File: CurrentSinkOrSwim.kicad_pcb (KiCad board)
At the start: 2 copper layers, 23 parts, among them P101 CONN_01X02, P102 CONN_01X03, P103 CONN_01X02, Q201 BUK9575, U201 LMV358IDT, U301 LMV358, U401 LM2931D-R

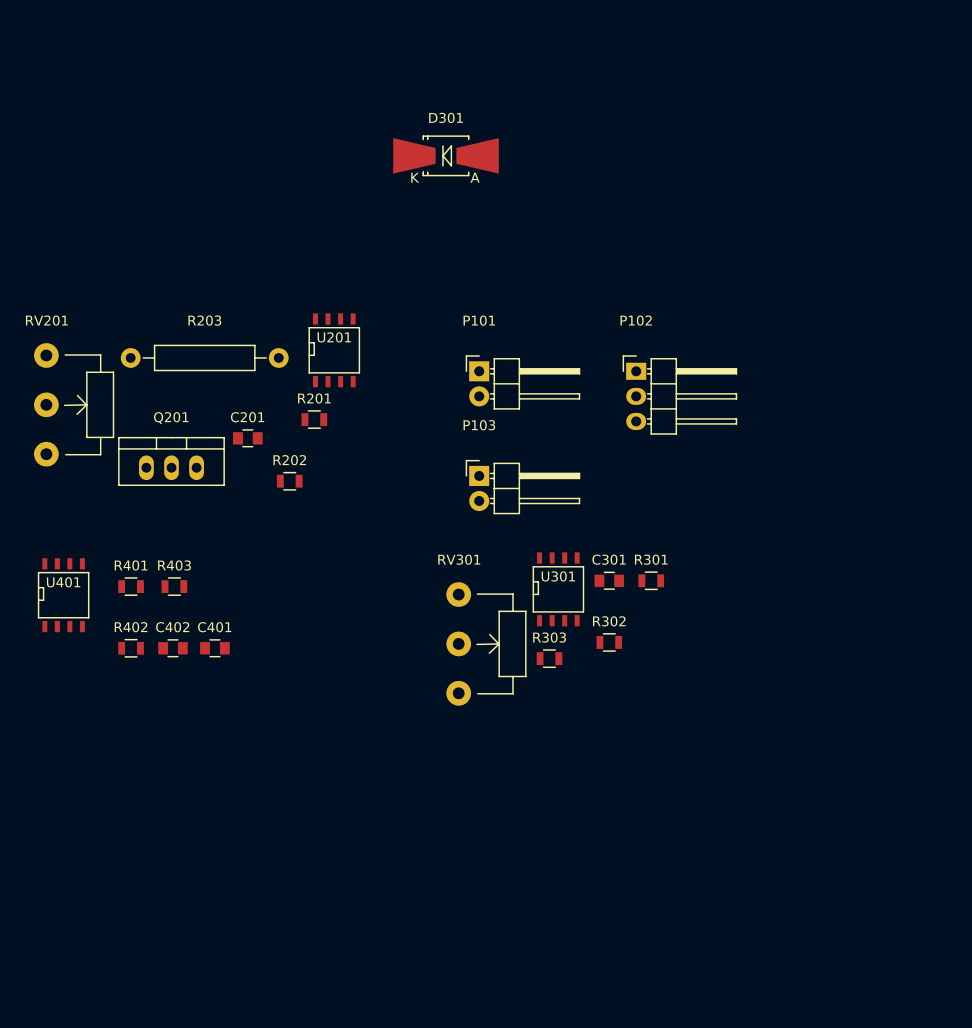
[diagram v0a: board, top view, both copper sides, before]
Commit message: Add heat sink footprint
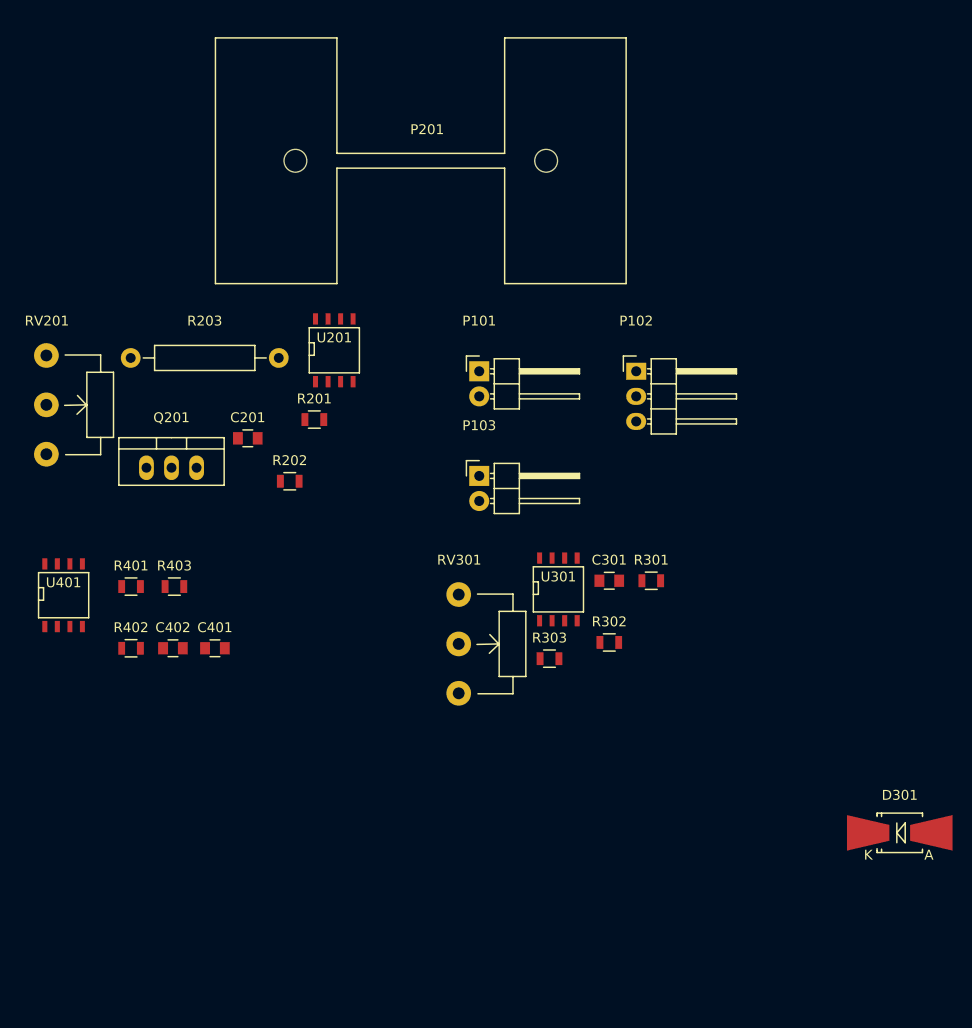
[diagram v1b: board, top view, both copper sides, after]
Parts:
- added P201: CONN_01X01, current:FA-T220-38E-ND, F.Cu at (125.5, 60.7)
- moved D301 82.6 mm to (174.0, 128.8)
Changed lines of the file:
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@@
     (tracks 0)
     (zones 0)
-    (modules 23)
+    (modules 24)
     (nets 20)
   )
@@
   )
   (module Diodes_SMD:SMB-SMC_Universal_Handsoldering (layer F.Cu)
-    (at 128.016 60.198)
+    (at 173.99 128.778)
     (descr "Diode, Universal, SMB, SMC, Handsoldering,")
     (tags "Diode Universal SMB SMC Handsoldering ")
@@
     )
   )
+  (module current:FA-T220-38E-ND (layer F.Cu)
+    (at 125.476 60.706)
+    (fp_text reference P201 (at 0.635 -3.175) (layer F.SilkS)
+      (effects (font (size 1 1) (thickness 0.15)))
+    )
+    (fp_text value CONN_01X01 (at 0 -5.715) (layer F.Fab)
+      (effects (font (size 1 1) (thickness 0.15)))
+    )
+    (fp_line (start -20.8153 12.4333) (end -8.509 12.4333) (layer F.SilkS) (width 0.15))
+    (fp_line (start 8.4836 12.4333) (end 20.7899 12.4333) (layer F.SilkS) (width 0.15))
+    (fp_line (start 8.4836 -12.4587) (end 20.7899 -12.4587) (layer F.SilkS) (width 0.15))
+    (fp_line (start -20.8153 -12.4587) (end -8.509 -12.4587) (layer F.SilkS) (width 0.15))
+    (fp_line (start 8.4836 12.4333) (end 8.4836 0.7366) (layer F.SilkS) (width 0.15))
+    (fp_line (start -8.509 12.4333) (end -8.509 0.7366) (layer F.SilkS) (width 0.15))
+    (fp_line (start -8.509 -0.762) (end -8.509 -12.4587) (layer F.SilkS) (width 0.15))
+    (fp_line (start 8.4836 -0.762) (end 8.4836 -12.4587) (layer F.SilkS) (width 0.15))
+    (fp_line (start -8.509 0.7366) (end 8.4836 0.7366) (layer F.SilkS) (width 0.15))
+    (fp_line (start -8.509 -0.762) (end 8.4836 -0.762) (layer F.SilkS) (width 0.15))
+    (fp_line (start -20.8153 -12.4587) (end -20.8153 12.4333) (layer F.SilkS) (width 0.15))
+    (fp_line (start 20.7899 12.4333) (end 20.7899 -12.4587) (layer F.SilkS) (width 0.15))
+    (pad "" np_thru_hole circle (at -12.7127 -0.0127) (size 2.3114 2.3114) (drill 2.3114) (layers *.Cu *.Mask))
+    (pad "" np_thru_hole circle (at 12.6873 -0.0127) (size 2.3114 2.3114) (drill 2.3114) (layers *.Cu *.Mask))
+  )
 )

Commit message: Remove extra erroneus LMV358
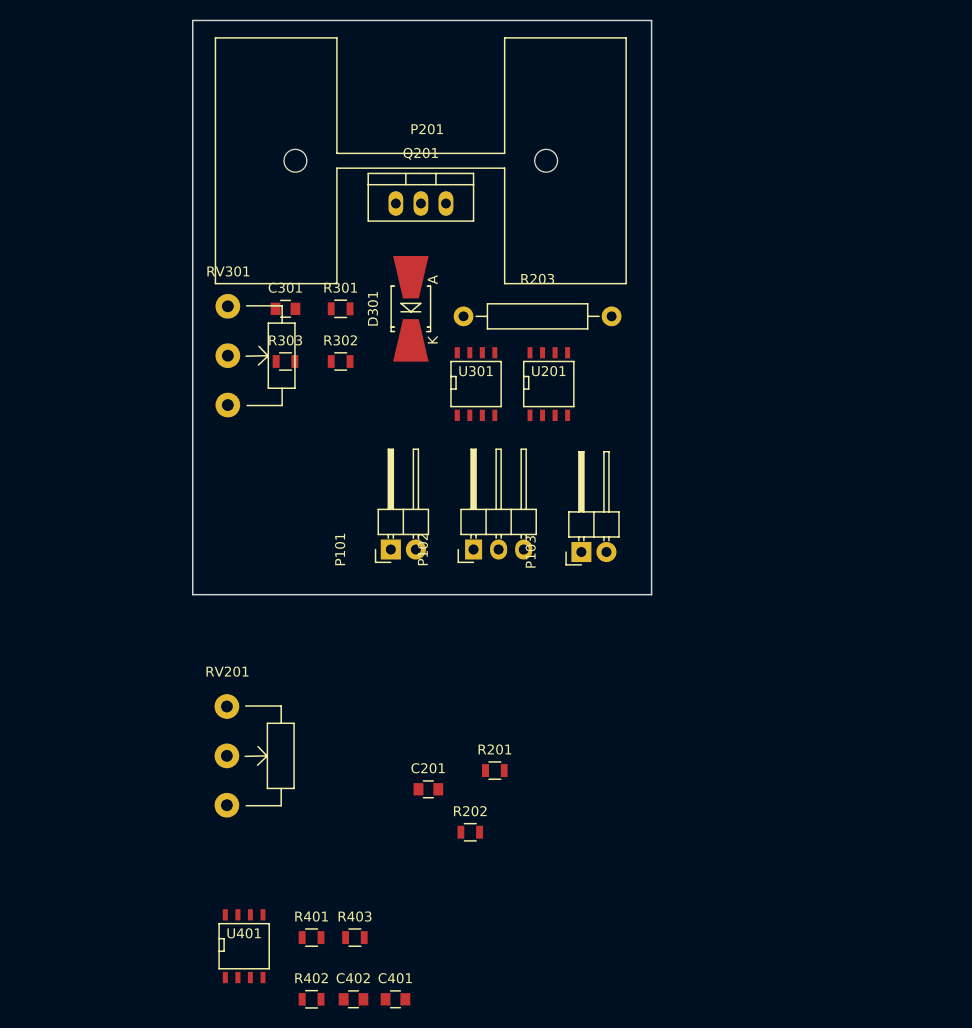
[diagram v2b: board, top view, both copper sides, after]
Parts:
- U201: value LMV358IDT -> LMV358
- moved D301 72.6 mm to (124.5, 75.7), turned to 90 degrees
- moved C301 42.8 mm to (111.8, 75.7)
- moved R301 41.8 mm to (117.3, 75.7)
- moved R303 40.3 mm to (111.8, 81.0)
- moved R201 40.0 mm to (133.0, 122.5)
- moved C401 40.0 mm to (122.9, 145.6)
- moved C402 40.0 mm to (118.6, 145.6)
- moved R202 40.0 mm to (130.5, 128.7)
- moved R401 40.0 mm to (114.4, 139.4)
- moved R402 40.0 mm to (114.4, 145.6)
- moved RV201 40.0 mm to (105.8, 116.0)
- moved C201 40.0 mm to (126.2, 124.4)
- moved R403 40.0 mm to (118.8, 139.4)
- moved U401 40.0 mm to (107.6, 140.3)
- moved R302 39.4 mm to (117.3, 81.0)
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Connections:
- U201 pad 5: (no net) -> Net-(R301-Pad1)
- U201 pad 6: (no net) -> Net-(R302-Pad2)
- U201 pad 7: (no net) -> Net-(D301-Pad1)
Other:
- board outline added: 46.5 x 58.2 mm

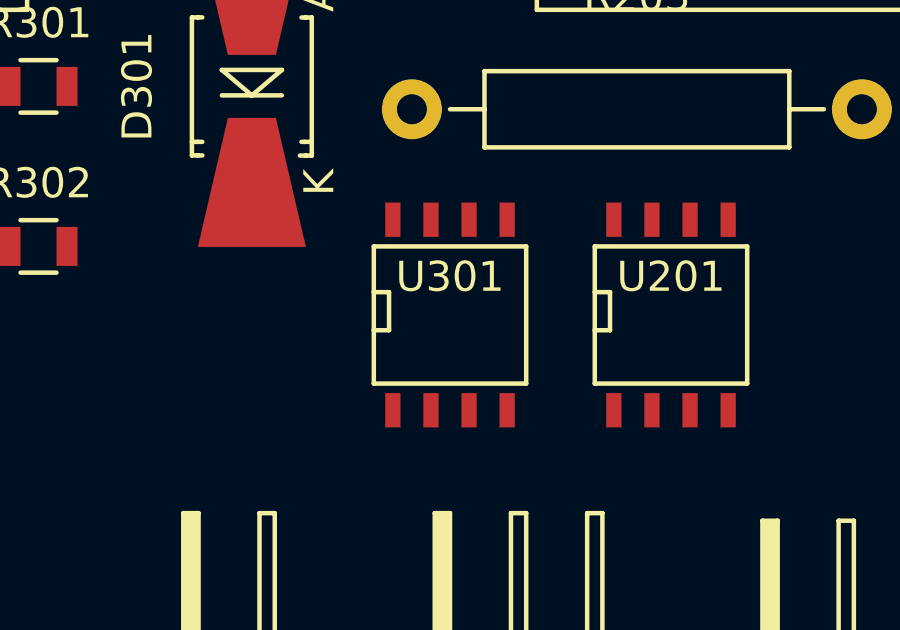
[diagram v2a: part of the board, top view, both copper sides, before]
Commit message: Forgot to update the layout after removing the extra LMV358
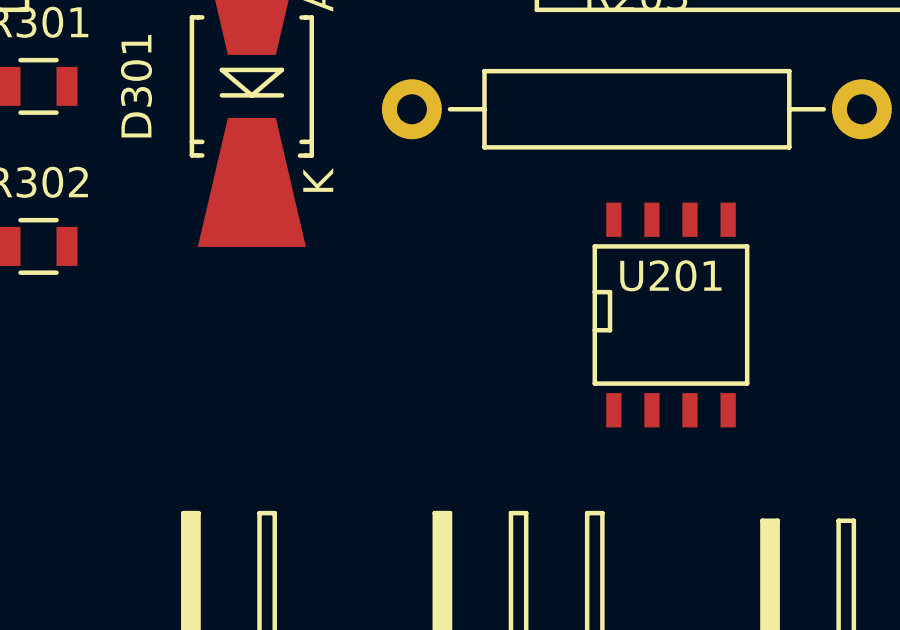
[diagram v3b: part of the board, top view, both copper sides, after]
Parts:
- removed U301: LMV358, SMD_Packages:SOIC-8-N
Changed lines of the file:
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@@
 (kicad_pcb (version 4) (host pcbnew 4.0.4+e1-6308~48~ubuntu14.04.1-stable)
   (general
-    (links 46)
-    (no_connects 46)
+    (links 41)
+    (no_connects 41)
     (area 102.286999 46.406999 148.919001 104.723001)
     (thickness 1.6)
@@
     (tracks 0)
     (zones 0)
-    (modules 24)
+    (modules 23)
     (nets 20)
   )
@@
     (model SMD_Packages.3dshapes/SOIC-8-N.wrl
       (at (xyz 0 0 0))
-      (scale (xyz 0.5 0.38 0.5))
-      (rotate (xyz 0 0 0))
-    )
-  )
-  (module SMD_Packages:SOIC-8-N (layer F.Cu)
-    (at 131.064 83.312)
-    (descr "Module Narrow CMS SOJ 8 pins large")
-    (tags "CMS SOJ")
-    (attr smd)
-    (fp_text reference U301 (at 0 -1.27) (layer F.SilkS)
-      (effects (font (size 1 1) (thickness 0.15)))
-    )
-    (fp_text value LMV358 (at 0 1.27) (layer F.Fab)
-      (effects (font (size 1 1) (thickness 0.15)))
-    )
-    (fp_line (start -2.54 -2.286) (end 2.54 -2.286) (layer F.SilkS) (width 0.15))
-    (fp_line (start 2.54 -2.286) (end 2.54 2.286) (layer F.SilkS) (width 0.15))
-    (fp_line (start 2.54 2.286) (end -2.54 2.286) (layer F.SilkS) (width 0.15))
-    (fp_line (start -2.54 2.286) (end -2.54 -2.286) (layer F.SilkS) (width 0.15))
-    (fp_line (start -2.54 -0.762) (end -2.032 -0.762) (layer F.SilkS) (width 0.15))
-    (fp_line (start -2.032 -0.762) (end -2.032 0.508) (layer F.SilkS) (width 0.15))
-    (fp_line (start -2.032 0.508) (end -2.54 0.508) (layer F.SilkS) (width 0.15))
-    (pad 8 smd rect (at -1.905 -3.175) (size 0.508 1.143) (layers F.Cu F.Paste F.Mask)
-      (net 1 2.7V))
-    (pad 7 smd rect (at -0.635 -3.175) (size 0.508 1.143) (layers F.Cu F.Paste F.Mask))
-    (pad 6 smd rect (at 0.635 -3.175) (size 0.508 1.143) (layers F.Cu F.Paste F.Mask))
-    (pad 5 smd rect (at 1.905 -3.175) (size 0.508 1.143) (layers F.Cu F.Paste F.Mask))
-    (pad 4 smd rect (at 1.905 3.175) (size 0.508 1.143) (layers F.Cu F.Paste F.Mask)
-      (net 2 GND))
-    (pad 3 smd rect (at 0.635 3.175) (size 0.508 1.143) (layers F.Cu F.Paste F.Mask)
-      (net 13 "Net-(R301-Pad1)"))
-    (pad 2 smd rect (at -0.635 3.175) (size 0.508 1.143) (layers F.Cu F.Paste F.Mask)
-      (net 15 "Net-(R302-Pad2)"))
-    (pad 1 smd rect (at -1.905 3.175) (size 0.508 1.143) (layers F.Cu F.Paste F.Mask)
-      (net 5 "Net-(D301-Pad1)"))
-    (model SMD_Packages.3dshapes/SOIC-8-N.wrl
-      (at (xyz 0 0 0))

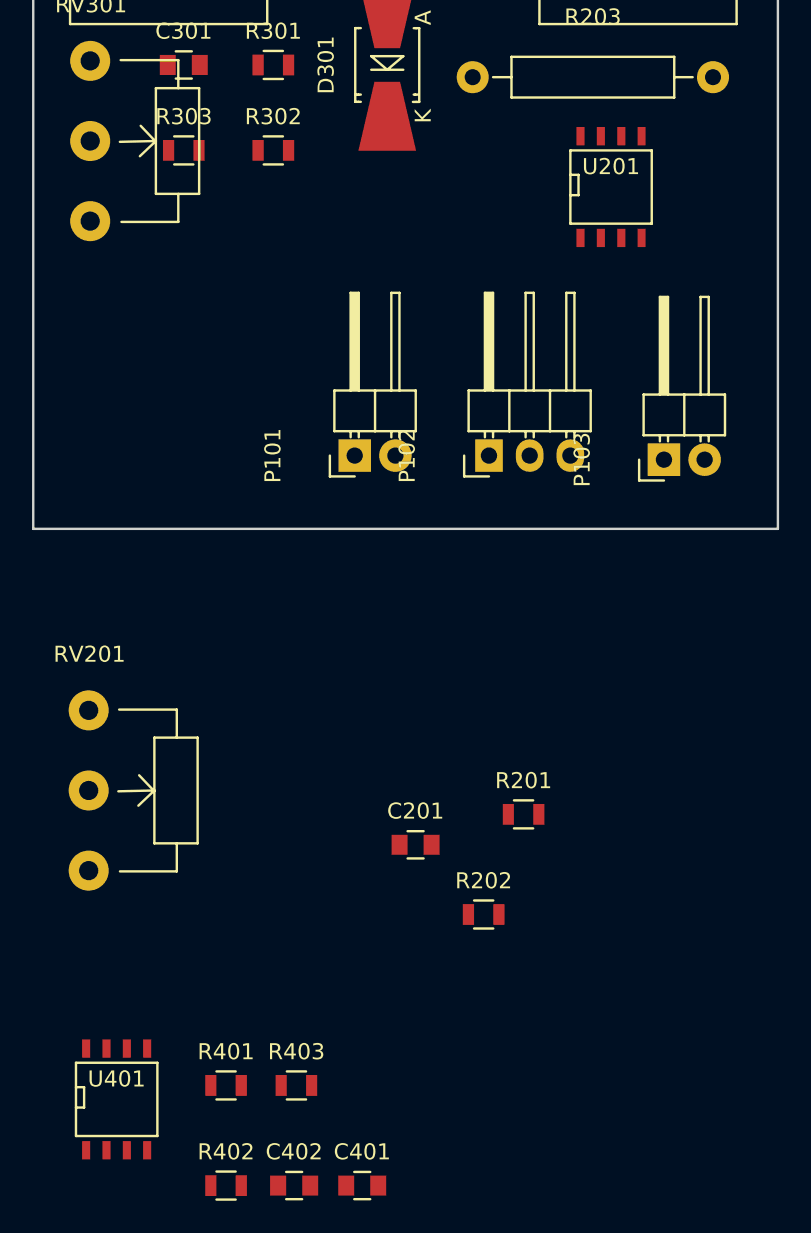
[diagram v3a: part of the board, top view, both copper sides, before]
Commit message: First pass of all components on the top layer of the board
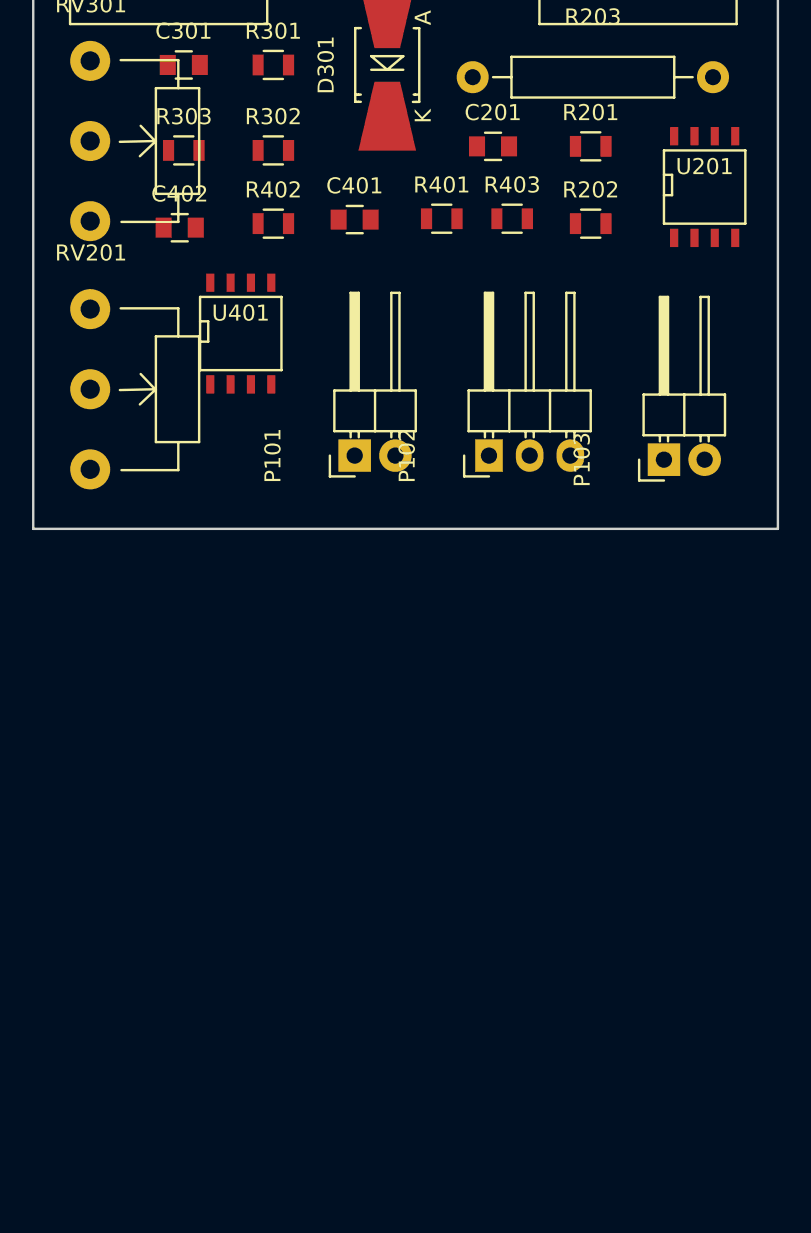
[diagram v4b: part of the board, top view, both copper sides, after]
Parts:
- moved C401 60.3 mm to (122.4, 85.3)
- moved C402 60.2 mm to (111.5, 85.9)
- moved R402 60.1 mm to (117.3, 85.6)
- moved R401 55.8 mm to (127.9, 85.3)
- moved R403 55.8 mm to (132.3, 85.3)
- moved U401 48.4 mm to (115.3, 92.5)
- moved C201 43.9 mm to (131.1, 80.8)
- moved R202 43.6 mm to (137.2, 85.6)
- moved R201 41.9 mm to (137.2, 80.8)
- moved RV201 25.0 mm to (105.9, 90.9)
- moved U201 5.84 mm to (144.3, 83.3)
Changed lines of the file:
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@@
     (links 41)
     (no_connects 41)
-    (area 102.286999 46.406999 148.919001 104.723001)
+    (area 102.286999 46.406999 148.919001 148.816)
     (thickness 1.6)
     (drawings 4)
@@
   )
   (module Capacitors_SMD:C_0805 (layer F.Cu)
-    (at 126.228571 124.371)
+    (at 131.064 80.772)
     (descr "Capacitor SMD 0805, reflow soldering, AVX (see smccp.pdf)")
     (tags "capacitor 0805")
@@
   )
   (module Capacitors_SMD:C_0805 (layer F.Cu)
-    (at 122.898571 145.641)
+    (at 122.428 85.344)
     (descr "Capacitor SMD 0805, reflow soldering, AVX (see smccp.pdf)")
     (tags "capacitor 0805")
@@
   )
   (module Capacitors_SMD:C_0805 (layer F.Cu)
-    (at 118.648571 145.641)
+    (at 111.506 85.852)
     (descr "Capacitor SMD 0805, reflow soldering, AVX (see smccp.pdf)")
     (tags "capacitor 0805")
@@
   )
   (module Resistors_SMD:R_0805 (layer F.Cu)
-    (at 132.968571 122.471)
+    (at 137.16 80.772)
     (descr "Resistor SMD 0805, reflow soldering, Vishay (see dcrcw.pdf)")
     (tags "resistor 0805")
@@
   )
   (module Resistors_SMD:R_0805 (layer F.Cu)
-    (at 130.478571 128.721)
+    (at 137.16 85.598)
     (descr "Resistor SMD 0805, reflow soldering, Vishay (see dcrcw.pdf)")
     (tags "resistor 0805")
@@
   )
   (module Resistors_SMD:R_0805 (layer F.Cu)
-    (at 114.398571 139.391)
+    (at 127.860571 85.289)
     (descr "Resistor SMD 0805, reflow soldering, Vishay (see dcrcw.pdf)")
     (tags "resistor 0805")
@@
   )
   (module Resistors_SMD:R_0805 (layer F.Cu)
-    (at 114.398571 145.641)
+    (at 117.348 85.598)
     (descr "Resistor SMD 0805, reflow soldering, Vishay (see dcrcw.pdf)")
     (tags "resistor 0805")
@@
   )
   (module Resistors_SMD:R_0805 (layer F.Cu)
-    (at 118.791428 139.391)
+    (at 132.253428 85.289)
     (descr "Resistor SMD 0805, reflow soldering, Vishay (see dcrcw.pdf)")
     (tags "resistor 0805")
@@
   )
   (module Potentiometers:Potentiometer_WirePads_largePads (layer F.Cu)
-    (at 105.823502 115.97858)
+    (at 105.918 90.932)
     (descr "Potentiometer, Wire Pads only, RevA, 30 July 2010,")
     (tags "Potentiometer, Wire Pads only, RevA, 30 July 2010,")
@@
   )
   (module SMD_Packages:SOIC-8-N (layer F.Cu)
-    (at 138.43 83.312)
+    (at 144.272 83.312)
     (descr "Module Narrow CMS SOJ 8 pins large")
     (tags "CMS SOJ")
@@
   )
   (module SMD_Packages:SOIC-8-N (layer F.Cu)
-    (at 107.57 140.2625)
+    (at 115.316 92.456)
     (descr "Module Narrow CMS SOJ 8 pins large")
     (tags "CMS SOJ")
